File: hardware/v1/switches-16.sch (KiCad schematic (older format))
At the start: 18 parts, among them P1 CONN_02X02, SW1 SWITCH_INV, SW10 SWITCH_INV, SW11 SWITCH_INV, SW12 SWITCH_INV, SW13 SWITCH_INV, SW14 SWITCH_INV, SW15 SWITCH_INV, SW16 SWITCH_INV, SW2 SWITCH_INV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

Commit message: Re-arrange switch connector pinout to simpler single-row header. Re-route the switch boards accordingly.
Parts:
- removed P1: CONN_02X02, Pin_Headers:Pin_Header_Angled_2x02, symbol CONN_02X02
- added P1: CONN_01X04, Pin_Headers:Pin_Header_Angled_1x04, symbol CONN_01X04
- added P2, P3, P4: CONN_01X03, Pin_Headers:Pin_Header_Straight_1x03, symbol CONN_01X03
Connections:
- wire segments 50 -> 53
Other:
- note removed: "ADDR 000"
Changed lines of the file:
@@
 LIBS:MCP23017
 LIBS:Pi2_Connector
-LIBS:v1-cache
+LIBS:switches-16-cache
 EELAYER 25 0
 EELAYER END
 $Descr A4 11693 8268
 encoding utf-8
-Sheet 25 27
+Sheet 1 1
 Title ""
 Date ""
@@
 NoConn ~ 5050 4500
 $Comp
-L VDD #PWR019
+L VDD #PWR01
 U 1 1 57A50722
 P 4700 4050
-F 0 "#PWR019" H 4700 3900 50  0001 C CNN
+F 0 "#PWR01" H 4700 3900 50  0001 C CNN
 F 1 "VDD" H 4700 4200 50  0000 C CNN
 F 2 "" H 4700 4050 50  0000 C CNN
@@
 $EndComp
 $Comp
-L GND #PWR020
+L GND #PWR02
 U 1 1 57A5073A
 P 4700 4250
-F 0 "#PWR020" H 4700 4000 50  0001 C CNN
+F 0 "#PWR02" H 4700 4000 50  0001 C CNN
 F 1 "GND" H 4700 4100 50  0000 C CNN
 F 2 "" H 4700 4250 50  0000 C CNN
@@
 	1    0    0    -1
 $EndComp
-Text Notes 6150 4850 0    60   ~ 0
-ADDR 000
-$Comp
-L GND #PWR021
+$Comp
+L GND #PWR03
 U 1 1 57A5092D
-P 6550 4550
-F 0 "#PWR021" H 6550 4300 50  0001 C CNN
-F 1 "GND" H 6550 4400 50  0000 C CNN
-F 2 "" H 6550 4550 50  0000 C CNN
-F 3 "" H 6550 4550 50  0000 C CNN
-	1    6550 4550
+P 7850 4550
+F 0 "#PWR03" H 7850 4300 50  0001 C CNN
+F 1 "GND" H 7850 4400 50  0000 C CNN
+F 2 "" H 7850 4550 50  0000 C CNN
+F 3 "" H 7850 4550 50  0000 C CNN
+	1    7850 4550
 	1    0    0    -1
 $EndComp
@@
 NoConn ~ 9450 2000
 Wire Wire Line
-	6550 4300 6550 4550
-Connection ~ 6550 4500
-Connection ~ 6550 4400
-Wire Wire Line
 	6550 4200 6650 4200
 Wire Wire Line
@@
 	4850 4150 4850 4100
 $Comp
-L GND #PWR022
+L GND #PWR04
 U 1 1 57A5373D
 P 850 1050
-F 0 "#PWR022" H 850 800 50  0001 C CNN
+F 0 "#PWR04" H 850 800 50  0001 C CNN
 F 1 "GND" H 850 900 50  0000 C CNN
 F 2 "" H 850 1050 50  0000 C CNN
@@
 Connection ~ 6950 1000
 $Comp
-L GND #PWR023
+L GND #PWR05
 U 1 1 57A54116
 P 6150 1100
-F 0 "#PWR023" H 6150 850 50  0001 C CNN
+F 0 "#PWR05" H 6150 850 50  0001 C CNN
 F 1 "GND" H 6150 950 50  0000 C CNN
 F 2 "" H 6150 1100 50  0000 C CNN
@@
 $EndComp
 $Comp
-L CONN_02X02 P1
-U 1 1 57A544DE
-P 1500 4800
-F 0 "P1" H 1500 4950 50  0000 C CNN
-F 1 "CONN_02X02" H 1500 4650 50  0000 C CNN
-F 2 "Pin_Headers:Pin_Header_Angled_2x02" H 1500 3600 50  0001 C CNN
-F 3 "" H 1500 3600 50  0000 C CNN
-	1    1500 4800
-	1    0    0    -1
-$EndComp
-$Comp
-L VDD #PWR024
+L VDD #PWR06
 U 1 1 57A547CB
-P 750 4700
-F 0 "#PWR024" H 750 4550 50  0001 C CNN
-F 1 "VDD" H 750 4850 50  0000 C CNN
-F 2 "" H 750 4700 50  0000 C CNN
-F 3 "" H 750 4700 50  0000 C CNN
-	1    750  4700
-	1    0    0    -1
-$EndComp
-$Comp
-L GND #PWR025
+P 1850 4200
+F 0 "#PWR06" H 1850 4050 50  0001 C CNN
+F 1 "VDD" H 1850 4350 50  0000 C CNN
+F 2 "" H 1850 4200 50  0000 C CNN
+F 3 "" H 1850 4200 50  0000 C CNN
+	1    1850 4200
+	1    0    0    -1
+$EndComp
+$Comp
+L GND #PWR07
 U 1 1 57A54805
-P 950 4600
-F 0 "#PWR025" H 950 4350 50  0001 C CNN
-F 1 "GND" H 950 4450 50  0000 C CNN
-F 2 "" H 950 4600 50  0000 C CNN
-F 3 "" H 950 4600 50  0000 C CNN
-	1    950  4600
-	1    0    0    -1
-$EndComp
-Wire Wire Line
-	950  4600 1250 4600
-Wire Wire Line
-	1250 4600 1250 4750
-Wire Wire Line
-	1250 4850 750  4850
-Wire Wire Line
-	750  4850 750  4700
-Text Label 1750 4850 0    60   ~ 0
+P 1850 3800
+F 0 "#PWR07" H 1850 3550 50  0001 C CNN
+F 1 "GND" H 1850 3650 50  0000 C CNN
+F 2 "" H 1850 3800 50  0000 C CNN
+F 3 "" H 1850 3800 50  0000 C CNN
+	1    1850 3800
+	1    0    0    -1
+$EndComp
+Text Label 2050 4300 2    60   ~ 0
 SDA
-Text Label 1750 4750 0    60   ~ 0
+Text Label 2050 4400 2    60   ~ 0
 SCK
 Text Label 5050 4300 2    60   ~ 0
@@
 	4700 4150 4700 4250
 $Comp
-L VDD #PWR026
+L VDD #PWR08
 U 1 1 57A54F92
 P 6650 4200
-F 0 "#PWR026" H 6650 4050 50  0001 C CNN
+F 0 "#PWR08" H 6650 4050 50  0001 C CNN
 F 1 "VDD" H 6650 4350 50  0000 C CNN
 F 2 "" H 6650 4200 50  0000 C CNN
@@
 Wire Wire Line
 	1400 3200 1400 2000
+$Comp
+L CONN_01X04 P1
+U 1 1 57A9BB33
+P 2250 4250
+F 0 "P1" H 2250 4500 50  0000 C CNN
+F 1 "CONN_01X04" V 2350 4250 50  0000 C CNN
+F 2 "Pin_Headers:Pin_Header_Angled_1x04" H 2250 3950 50  0000 C CNN
+F 3 "" H 2250 4250 50  0000 C CNN
+	1    2250 4250
+	1    0    0    -1
+$EndComp
+$Comp
+L CONN_01X03 P2
+U 1 1 57A9C3B9
+P 6750 4400
+F 0 "P2" H 6750 4600 50  0000 C CNN
+F 1 "CONN_01X03" V 6850 4400 50  0000 C CNN
+F 2 "Pin_Headers:Pin_Header_Straight_1x03" H 6750 4400 50  0001 C CNN
+F 3 "" H 6750 4400 50  0000 C CNN
+	1    6750 4400
+	1    0    0    -1
+$EndComp
+$Comp
+L CONN_01X03 P4
+U 1 1 57A9C500
+P 8050 4400
+F 0 "P4" H 8050 4600 50  0000 C CNN
+F 1 "CONN_01X03" V 8150 4400 50  0000 C CNN
+F 2 "Pin_Headers:Pin_Header_Straight_1x03" H 8050 4400 50  0001 C CNN
+F 3 "" H 8050 4400 50  0000 C CNN
+	1    8050 4400
+	1    0    0    -1
+$EndComp
+Wire Wire Line
+	7850 4550 7850 4300
+Wire Wire Line
+	7850 4500 7850 4400
+Connection ~ 7850 4400
+Connection ~ 7850 4500
+$Comp
+L VDD #PWR09
+U 1 1 57A9C86C
+P 7200 4150
+F 0 "#PWR09" H 7200 4000 50  0001 C CNN
+F 1 "VDD" H 7200 4300 50  0000 C CNN
+F 2 "" H 7200 4150 50  0000 C CNN
+F 3 "" H 7200 4150 50  0000 C CNN
+	1    7200 4150
+	1    0    0    -1
+$EndComp
+Wire Wire Line
+	7200 4150 7200 4300
+Wire Wire Line
+	7200 4300 7300 4300
+$Comp
+L CONN_01X03 P3
+U 1 1 57A9CB31
+P 7500 4400
+F 0 "P3" H 7500 4600 50  0000 C CNN
+F 1 "CONN_01X03" V 7600 4400 50  0000 C CNN
+F 2 "Pin_Headers:Pin_Header_Straight_1x03" H 7500 4400 50  0001 C CNN
+F 3 "" H 7500 4400 50  0000 C CNN
+	1    7500 4400
+	1    0    0    -1
+$EndComp
+Wire Wire Line
+	7300 4300 7300 4500
+Connection ~ 7300 4400
+Connection ~ 7300 4300
+Wire Wire Line
+	1850 4200 2050 4200
+Wire Wire Line
+	1850 3800 2050 3800
+Wire Wire Line
+	2050 3800 2050 4100
 $EndSCHEMATC

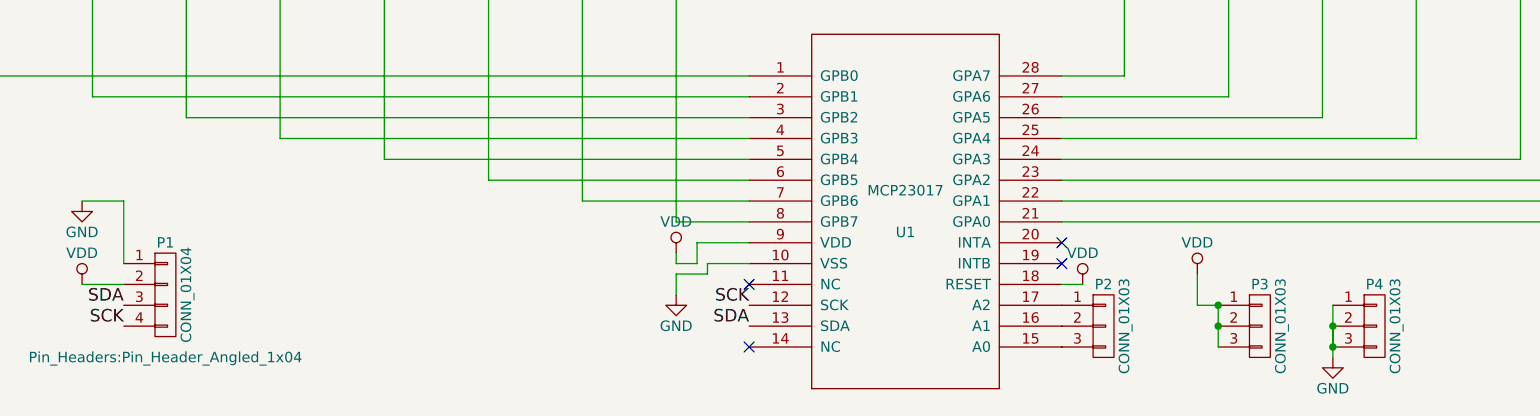
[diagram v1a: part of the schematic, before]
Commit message: Add new schematics for additional switch boards
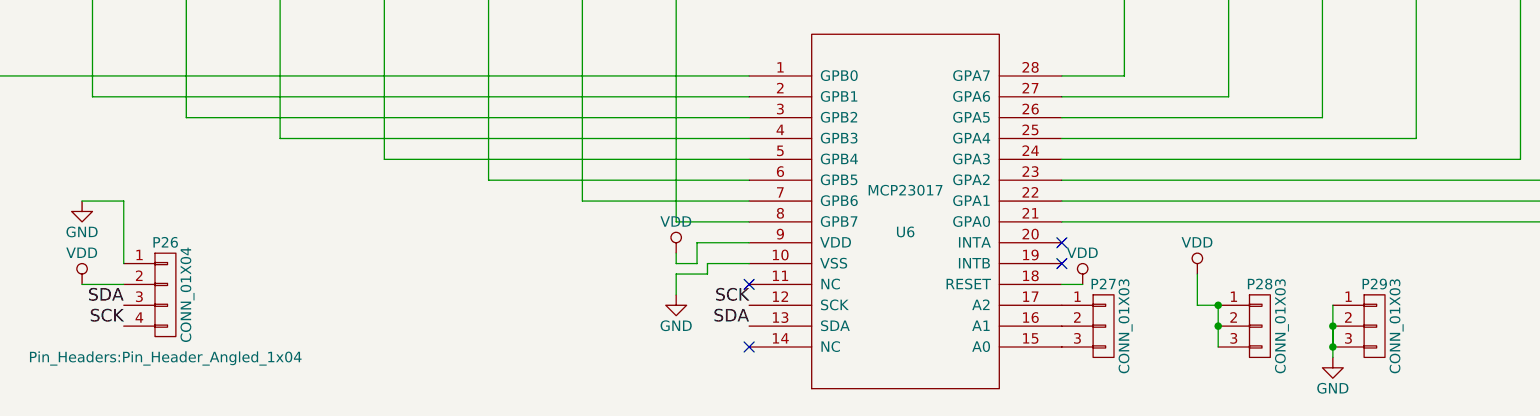
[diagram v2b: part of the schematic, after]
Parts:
- renumbered P1 to P26, P2 to P27, P3 to P28, P4 to P29, U1 to U6
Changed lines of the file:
@@
 LIBS:MCP23017
 LIBS:Pi2_Connector
-LIBS:switches-16-cache
+LIBS:v1-cache
 EELAYER 25 0
 EELAYER END
 $Descr A4 11693 8268
 encoding utf-8
-Sheet 1 1
+Sheet 25 30
 Title ""
 Date ""
@@
 NoConn ~ 5050 4500
 $Comp
-L VDD #PWR01
+L VDD #PWR23
 U 1 1 57A50722
 P 4700 4050
-F 0 "#PWR01" H 4700 3900 50  0001 C CNN
+F 0 "#PWR23" H 4700 3900 50  0001 C CNN
 F 1 "VDD" H 4700 4200 50  0000 C CNN
 F 2 "" H 4700 4050 50  0000 C CNN
@@
 $EndComp
 $Comp
-L GND #PWR02
+L GND #PWR24
 U 1 1 57A5073A
 P 4700 4250
-F 0 "#PWR02" H 4700 4000 50  0001 C CNN
+F 0 "#PWR24" H 4700 4000 50  0001 C CNN
 F 1 "GND" H 4700 4100 50  0000 C CNN
 F 2 "" H 4700 4250 50  0000 C CNN
@@
 $EndComp
 $Comp
-L GND #PWR03
+L GND #PWR28
 U 1 1 57A5092D
 P 7850 4550
-F 0 "#PWR03" H 7850 4300 50  0001 C CNN
+F 0 "#PWR28" H 7850 4300 50  0001 C CNN
 F 1 "GND" H 7850 4400 50  0000 C CNN
 F 2 "" H 7850 4550 50  0000 C CNN
@@
 	4850 4150 4850 4100
 $Comp
-L GND #PWR04
+L GND #PWR20
 U 1 1 57A5373D
 P 850 1050
-F 0 "#PWR04" H 850 800 50  0001 C CNN
+F 0 "#PWR20" H 850 800 50  0001 C CNN
 F 1 "GND" H 850 900 50  0000 C CNN
 F 2 "" H 850 1050 50  0000 C CNN
@@
 Connection ~ 6950 1000
 $Comp
-L GND #PWR05
+L GND #PWR25
 U 1 1 57A54116
 P 6150 1100
-F 0 "#PWR05" H 6150 850 50  0001 C CNN
+F 0 "#PWR25" H 6150 850 50  0001 C CNN
 F 1 "GND" H 6150 950 50  0000 C CNN
 F 2 "" H 6150 1100 50  0000 C CNN
@@
 $EndComp
 $Comp
-L VDD #PWR06
+L VDD #PWR22
 U 1 1 57A547CB
 P 1850 4200
-F 0 "#PWR06" H 1850 4050 50  0001 C CNN
+F 0 "#PWR22" H 1850 4050 50  0001 C CNN
 F 1 "VDD" H 1850 4350 50  0000 C CNN
 F 2 "" H 1850 4200 50  0000 C CNN
@@
 $EndComp
 $Comp
-L GND #PWR07
+L GND #PWR21
 U 1 1 57A54805
 P 1850 3800
-F 0 "#PWR07" H 1850 3550 50  0001 C CNN
+F 0 "#PWR21" H 1850 3550 50  0001 C CNN
 F 1 "GND" H 1850 3650 50  0000 C CNN
 F 2 "" H 1850 3800 50  0000 C CNN
@@
 	4700 4150 4700 4250
 $Comp
-L VDD #PWR08
+L VDD #PWR26
 U 1 1 57A54F92
 P 6650 4200
-F 0 "#PWR08" H 6650 4050 50  0001 C CNN
+F 0 "#PWR26" H 6650 4050 50  0001 C CNN
 F 1 "VDD" H 6650 4350 50  0000 C CNN
 F 2 "" H 6650 4200 50  0000 C CNN
@@
 $EndComp
 $Comp
-L MCP23017 U1
+L MCP23017 U6
 U 1 1 57A494D1
 P 5800 3850
-F 0 "U1" H 5800 3750 50  0000 C CNN
+F 0 "U6" H 5800 3750 50  0000 C CNN
 F 1 "MCP23017" H 5800 3950 50  0000 C CNN
 F 2 "DIL28:DIL28" H 5800 3850 50  0001 C CNN
@@
 	1400 3200 1400 2000
 $Comp
-L CONN_01X04 P1
+L CONN_01X04 P26
 U 1 1 57A9BB33
 P 2250 4250
-F 0 "P1" H 2250 4500 50  0000 C CNN
+F 0 "P26" H 2250 4500 50  0000 C CNN
 F 1 "CONN_01X04" V 2350 4250 50  0000 C CNN
 F 2 "Pin_Headers:Pin_Header_Angled_1x04" H 2250 3950 50  0000 C CNN
@@
 $EndComp
 $Comp
-L CONN_01X03 P2
+L CONN_01X03 P27
 U 1 1 57A9C3B9
 P 6750 4400
-F 0 "P2" H 6750 4600 50  0000 C CNN
+F 0 "P27" H 6750 4600 50  0000 C CNN
 F 1 "CONN_01X03" V 6850 4400 50  0000 C CNN
 F 2 "Pin_Headers:Pin_Header_Straight_1x03" H 6750 4400 50  0001 C CNN
@@
 $EndComp
 $Comp
-L CONN_01X03 P4
+L CONN_01X03 P29
 U 1 1 57A9C500
 P 8050 4400
-F 0 "P4" H 8050 4600 50  0000 C CNN
+F 0 "P29" H 8050 4600 50  0000 C CNN
 F 1 "CONN_01X03" V 8150 4400 50  0000 C CNN
 F 2 "Pin_Headers:Pin_Header_Straight_1x03" H 8050 4400 50  0001 C CNN
@@
 Connection ~ 7850 4500
 $Comp
-L VDD #PWR09
+L VDD #PWR27
 U 1 1 57A9C86C
 P 7200 4150
-F 0 "#PWR09" H 7200 4000 50  0001 C CNN
+F 0 "#PWR27" H 7200 4000 50  0001 C CNN
 F 1 "VDD" H 7200 4300 50  0000 C CNN
 F 2 "" H 7200 4150 50  0000 C CNN
@@
 	7200 4300 7300 4300
 $Comp
-L CONN_01X03 P3
+L CONN_01X03 P28
 U 1 1 57A9CB31
 P 7500 4400
-F 0 "P3" H 7500 4600 50  0000 C CNN
+F 0 "P28" H 7500 4600 50  0000 C CNN
 F 1 "CONN_01X03" V 7600 4400 50  0000 C CNN
 F 2 "Pin_Headers:Pin_Header_Straight_1x03" H 7500 4400 50  0001 C CNN
